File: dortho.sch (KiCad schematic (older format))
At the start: 129 parts, among them SW1 SW_Push, U1 ATmega32U4-AU, Y1 16MHz

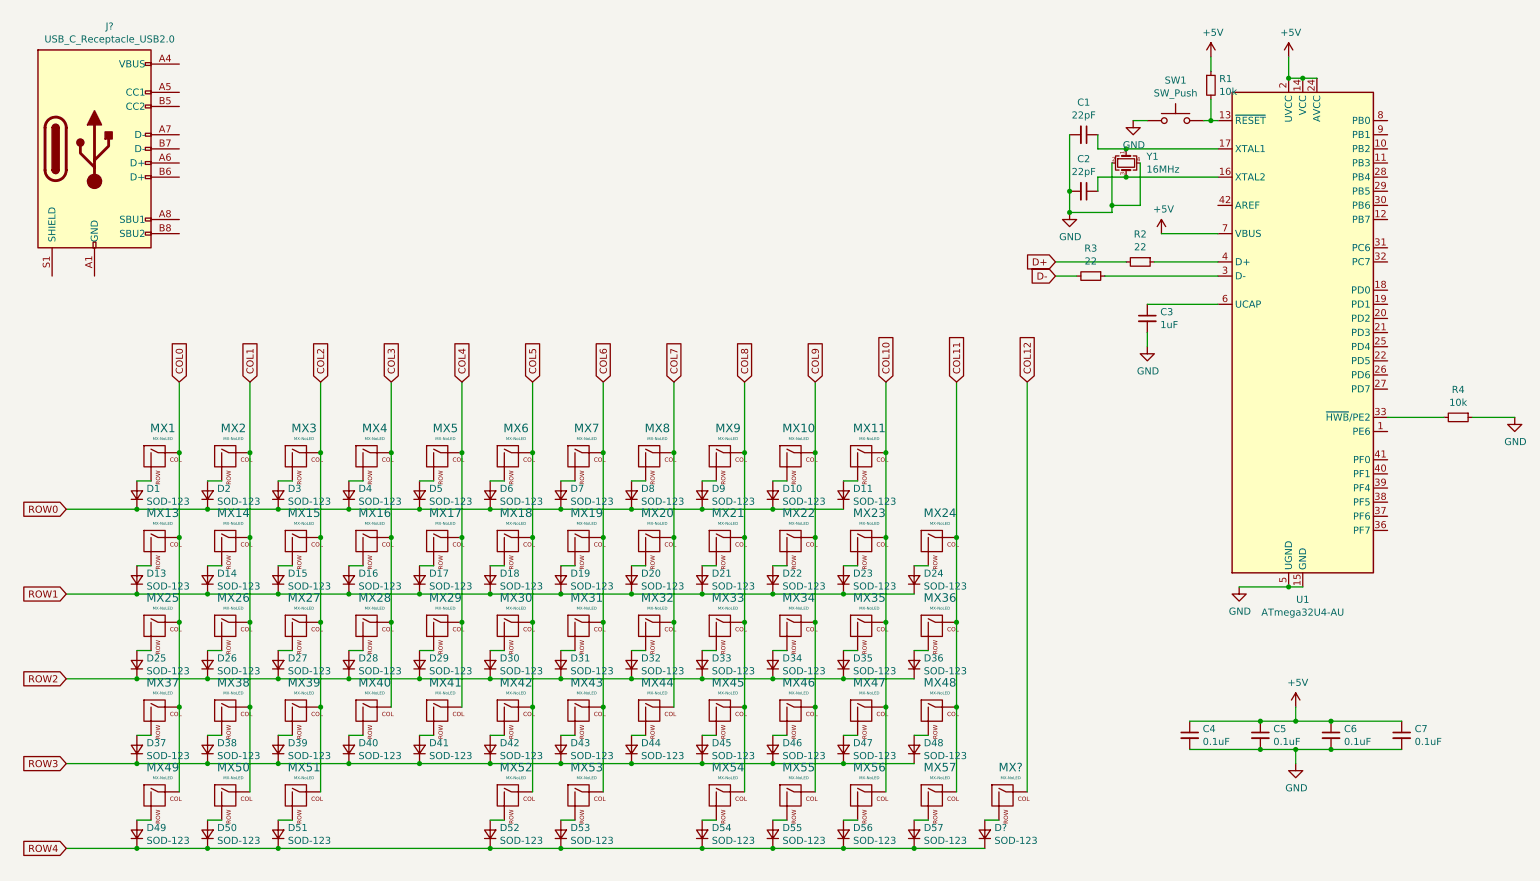
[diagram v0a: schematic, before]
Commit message: Clear switch matrix
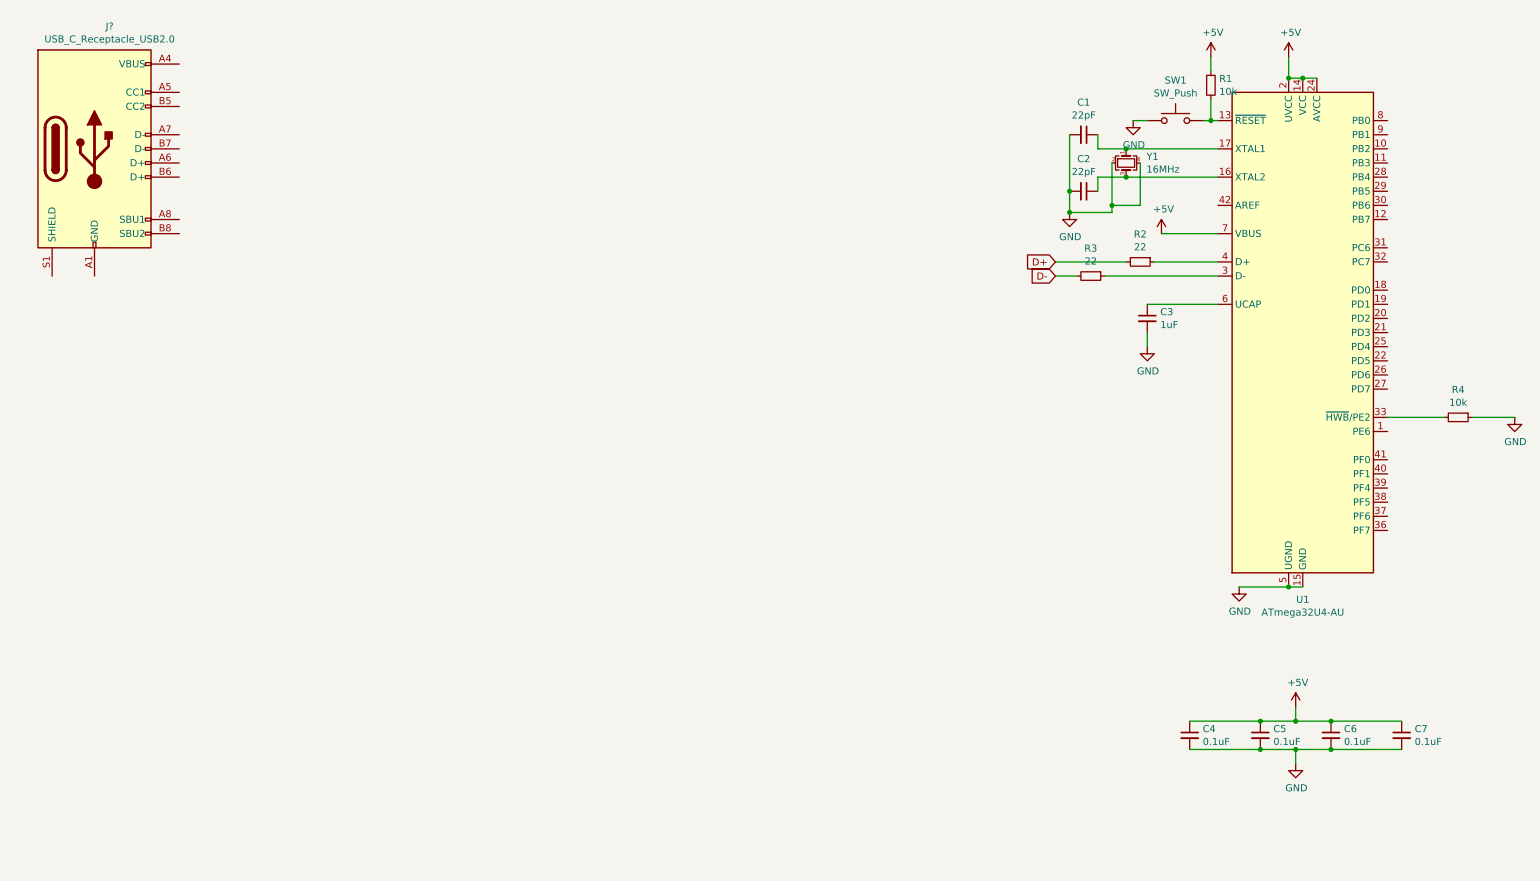
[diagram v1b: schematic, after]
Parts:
- removed D1, D10, D11, D13, D14, D15, D16, D17, D18, D19, D2, D20, D21, D22, D23, D24, D25, D26, D27, D28, D29, D3, D30, D31, D32, D33, D34, D35, D36, D37, D38, D39, D4, D40, D41, D42, D43, D44, D45, D46, D47, D48, D49, D5, D50, D51, D52, D53, D54, D55, D56, D57, D6, D7, D8, D9, D?: SOD-123, Diode_SMD:D_SOD-123, symbol Device:D_Small
- removed MX1, MX10, MX11, MX13, MX14, MX15, MX16, MX17, MX18, MX19, MX2, MX20, MX21, MX22, MX23, MX24, MX25, MX26, MX27, MX28, MX29, MX3, MX30, MX31, MX32, MX33, MX34, MX35, MX36, MX37, MX38, MX39, MX4, MX40, MX41, MX42, MX43, MX44, MX45, MX46, MX47, MX48, MX49, MX5, MX50, MX51, MX52, MX53, MX54, MX55, MX56, MX57, MX6, MX7, MX8, MX9, MX?: MX-NoLED, MX_Alps_Hybrid:MX-1U-NoLED, symbol MX_Alps_Hybrid:MX-NoLED

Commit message: Finish switch matrix
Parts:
- added D? (x73): D_Small, symbol Device:D_Small
- added MX? (x73): MX-NoLED, symbol MX_Alps_Hybrid:MX-NoLED
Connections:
- new net: D?.2 (A), MX?.2 (ROW) (x73)
- new net COL0: MX?.1 (COL), MX?.1 (COL), MX?.1 (COL), MX?.1 (COL), MX?.1 (COL)
- new net COL1: MX?.1 (COL), MX?.1 (COL), MX?.1 (COL), MX?.1 (COL), MX?.1 (COL)
- new net COL10: MX?.1 (COL), MX?.1 (COL), MX?.1 (COL), MX?.1 (COL), MX?.1 (COL)
- new net COL11: MX?.1 (COL), MX?.1 (COL), MX?.1 (COL), MX?.1 (COL), MX?.1 (COL)
- new net COL12: MX?.1 (COL), MX?.1 (COL), MX?.1 (COL), MX?.1 (COL), MX?.1 (COL)
- new net COL13: MX?.1 (COL), MX?.1 (COL), MX?.1 (COL), MX?.1 (COL), MX?.1 (COL)
- new net COL14: MX?.1 (COL), MX?.1 (COL), MX?.1 (COL), MX?.1 (COL)
- new net COL2: MX?.1 (COL), MX?.1 (COL), MX?.1 (COL), MX?.1 (COL), MX?.1 (COL)
- new net COL3: MX?.1 (COL), MX?.1 (COL), MX?.1 (COL), MX?.1 (COL), MX?.1 (COL)
- new net COL4: MX?.1 (COL), MX?.1 (COL), MX?.1 (COL), MX?.1 (COL), MX?.1 (COL)
- new net COL5: MX?.1 (COL), MX?.1 (COL), MX?.1 (COL), MX?.1 (COL), MX?.1 (COL)
- new net COL6: MX?.1 (COL), MX?.1 (COL), MX?.1 (COL), MX?.1 (COL)
- new net COL7: MX?.1 (COL), MX?.1 (COL), MX?.1 (COL), MX?.1 (COL), MX?.1 (COL)
- new net COL8: MX?.1 (COL), MX?.1 (COL), MX?.1 (COL), MX?.1 (COL), MX?.1 (COL)
- new net COL9: MX?.1 (COL), MX?.1 (COL), MX?.1 (COL), MX?.1 (COL), MX?.1 (COL)
- new net ROW0: D?.1 (K), D?.1 (K), D?.1 (K), D?.1 (K), D?.1 (K), D?.1 (K), D?.1 (K), D?.1 (K), D?.1 (K), D?.1 (K), D?.1 (K), D?.1 (K), D?.1 (K), D?.1 (K), D?.1 (K)
- new net ROW1: D?.1 (K), D?.1 (K), D?.1 (K), D?.1 (K), D?.1 (K), D?.1 (K), D?.1 (K), D?.1 (K), D?.1 (K), D?.1 (K), D?.1 (K), D?.1 (K), D?.1 (K), D?.1 (K), D?.1 (K)
- new net ROW2: D?.1 (K), D?.1 (K), D?.1 (K), D?.1 (K), D?.1 (K), D?.1 (K), D?.1 (K), D?.1 (K), D?.1 (K), D?.1 (K), D?.1 (K), D?.1 (K), D?.1 (K), D?.1 (K), D?.1 (K)
- new net ROW3: D?.1 (K), D?.1 (K), D?.1 (K), D?.1 (K), D?.1 (K), D?.1 (K), D?.1 (K), D?.1 (K), D?.1 (K), D?.1 (K), D?.1 (K), D?.1 (K), D?.1 (K), D?.1 (K), D?.1 (K)
- new net ROW4: D?.1 (K), D?.1 (K), D?.1 (K), D?.1 (K), D?.1 (K), D?.1 (K), D?.1 (K), D?.1 (K), D?.1 (K), D?.1 (K), D?.1 (K), D?.1 (K), D?.1 (K)

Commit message: Finishing with type C
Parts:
- added D?: D_Schottky, symbol Device:D_Schottky
- added FB?: Ferrite_Bead_Small, symbol Device:Ferrite_Bead_Small
- added R? (x2): 5.1k, symbol Device:R
- added TH?: Thermistor, symbol Device:Thermistor
- added U?: USBLC6-2SC6, Package_TO_SOT_SMD:SOT-23-6, symbol Power_Protection:USBLC6-2SC6
- gave numbers to parts that had none: 147
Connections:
- net +5V: now also J1.A4 (VBUS), J1.A9 (VBUS), J1.B4 (VBUS), J1.B9 (VBUS), D?.1 (K), TH?.2, U?.5 (VBUS)
- net D+: now also J1.A7 (D-), J1.B7 (D-)
- net D-: now also J1.A6 (D+), J1.B6 (D+)
- net GND: now also J1.A1 (GND), J1.A12 (GND), J1.B1 (GND), J1.B12 (GND), FB?.1, R?.1, R?.1, U?.2 (GND)
- net at J1.A5 (CC1): now also R?.2
- net at J1.B5 (CC2): now also R?.2
- net at J1.S1 (SHIELD): now also FB?.2
- new net: D?.2 (A), TH?.1

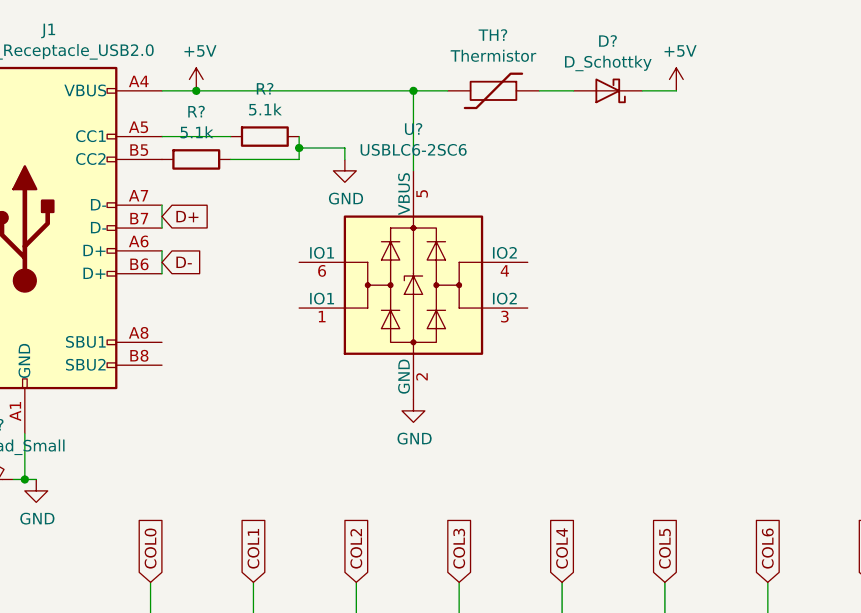
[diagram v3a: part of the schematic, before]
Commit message: Finish type C connection
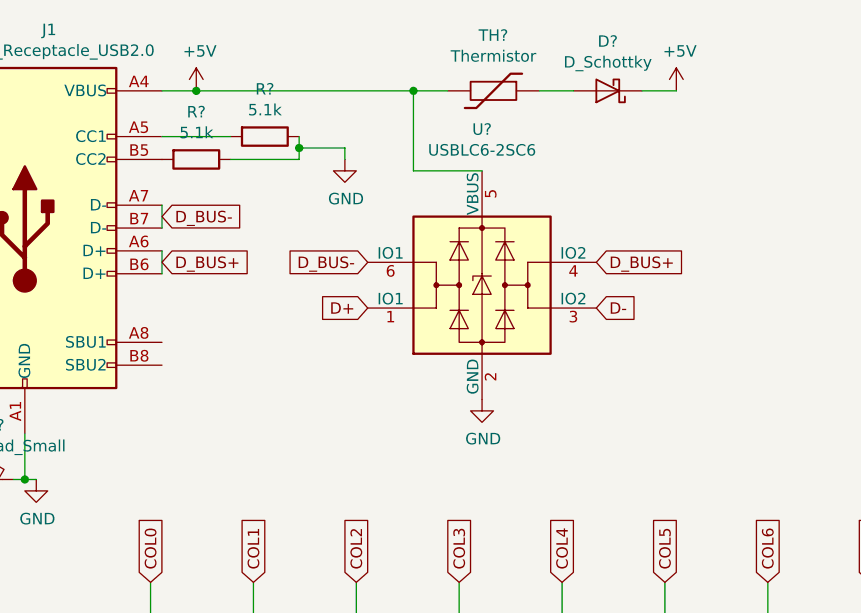
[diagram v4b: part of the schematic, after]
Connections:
- net D+: now also U?.1 (IO1); no longer J1.A7 (D-), J1.B7 (D-)
- net D-: now also U?.3 (IO2); no longer J1.A6 (D+), J1.B6 (D+)
- net D_BUS+: now reaches U?.4 (IO2)
- net D_BUS+: now also J1.A6 (D+), J1.B6 (D+)
- net D_BUS-: now reaches U?.6 (IO1)
- net D_BUS-: now also J1.A7 (D-), J1.B7 (D-)
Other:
- moved on the sheet: U?
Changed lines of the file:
@@
 	1    0    0    -1
 $EndComp
-$Comp
-L Power_Protection:USBLC6-2SC6 U?
-U 1 1 630D6912
-P 2700 1700
-F 0 "U?" H 2700 2381 50  0000 C CNN
-F 1 "USBLC6-2SC6" H 2700 2290 50  0000 C CNN
-F 2 "Package_TO_SOT_SMD:SOT-23-6" H 1950 2100 50  0001 C CNN
-F 3 "http://www2.st.com/resource/en/datasheet/CD00050750.pdf" H 2900 2050 50  0001 C CNN
-	1    2700 1700
-	1    0    0    -1
-$EndComp
-Text GLabel 1600 1600 2    50   Input ~ 0
-D-
 Wire Wire Line
 	1600 1550 1600 1650
-Text GLabel 1600 1400 2    50   Input ~ 0
-D+
 Wire Wire Line
 	1600 1350 1600 1450
@@
 	0    1    1    0
 $EndComp
-Wire Wire Line
-	1750 850  2700 850
 Connection ~ 1750 850
-Wire Wire Line
-	2700 1200 2700 850
-Connection ~ 2700 850
-Wire Wire Line
-	2700 850  2850 850
-$Comp
-L power:GND #PWR?
-U 1 1 632ED364
-P 2700 2200
-F 0 "#PWR?" H 2700 1950 50  0001 C CNN
-F 1 "GND" H 2705 2027 50  0000 C CNN
-F 2 "" H 2700 2200 50  0001 C CNN
-F 3 "" H 2700 2200 50  0001 C CNN
-	1    2700 2200
-	1    0    0    -1
-$EndComp
 $Comp
 L Device:D_Schottky D?
@@
 Wire Wire Line
 	3700 850  3850 850
+Text GLabel 1600 1400 2    50   Input ~ 0
+D_BUS-
+Text GLabel 1600 1600 2    50   Input ~ 0
+D_BUS+
+Connection ~ 2700 850
+Wire Wire Line
+	2700 850  2850 850
+Wire Wire Line
+	1750 850  2700 850
+Wire Wire Line
+	2700 1200 2700 850
+Wire Wire Line
+	2700 1200 3000 1200
+Text GLabel 3500 1600 2    50   Input ~ 0
+D_BUS+
+Text GLabel 2500 1600 0    50   Input ~ 0
+D_BUS-
+$Comp
+L power:GND #PWR?
+U 1 1 632ED364
+P 3000 2200
+F 0 "#PWR?" H 3000 1950 50  0001 C CNN
+F 1 "GND" H 3005 2027 50  0000 C CNN
+F 2 "" H 3000 2200 50  0001 C CNN
+F 3 "" H 3000 2200 50  0001 C CNN
+	1    3000 2200
+	1    0    0    -1
+$EndComp
+Text GLabel 2500 1800 0    50   Input ~ 0
+D+
+Text GLabel 3500 1800 2    50   Input ~ 0
+D-
+$Comp
+L Power_Protection:USBLC6-2SC6 U?
+U 1 1 630D6912
+P 3000 1700
+F 0 "U?" H 3000 2381 50  0000 C CNN
+F 1 "USBLC6-2SC6" H 3000 2290 50  0000 C CNN
+F 2 "Package_TO_SOT_SMD:SOT-23-6" H 2250 2100 50  0001 C CNN
+F 3 "http://www2.st.com/resource/en/datasheet/CD00050750.pdf" H 3200 2050 50  0001 C CNN
+	1    3000 1700
+	1    0    0    -1
+$EndComp
 $EndSCHEMATC

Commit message: Modify VCC
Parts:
- gave numbers to parts that had none: 6
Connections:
- net +5V: no longer U1.14 (VCC), U1.2 (UVCC), U1.24 (AVCC), U1.34 (VCC), U1.44 (AVCC)
- net COL0: now also U1.22 (PD5)
- net COL1: now also U1.25 (PD4)
- net COL10: now also U1.37 (PF6)
- net COL11: now also U1.38 (PF5)
- net COL12: now also U1.39 (PF4)
- net COL13: now also U1.40 (PF1)
- net COL14: now also U1.41 (PF0)
- net COL2: now also U1.26 (PD6)
- net COL3: now also U1.27 (PD7)
- net COL4: now also U1.28 (PB4)
- net COL5: now also U1.29 (PB5)
- net COL6: now also U1.30 (PB6)
- net COL7: now also U1.31 (PC6)
- net COL8: now also U1.32 (PC7)
- net COL9: now also U1.36 (PF7)
- net ROW0: now also U1.1 (PE6)
- net ROW1: now also U1.8 (PB0)
- net ROW2: now also U1.9 (PB1)
- net ROW3: now also U1.10 (PB2)
- net ROW4: now also U1.11 (PB3)
- new net: U1.14 (VCC), U1.2 (UVCC), U1.24 (AVCC), U1.34 (VCC), U1.44 (AVCC)
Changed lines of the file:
@@
 L power:+5V #PWR0101
 U 1 1 624280D8
-P 9450 800
-F 0 "#PWR0101" H 9450 650 50  0001 C CNN
-F 1 "+5V" H 9465 973 50  0000 C CNN
-F 2 "" H 9450 800 50  0001 C CNN
-F 3 "" H 9450 800 50  0001 C CNN
-	1    9450 800
-	1    0    0    -1
-$EndComp
-Wire Wire Line
-	9450 800  9450 950
+P 9450 700
+F 0 "#PWR0101" H 9450 550 50  0001 C CNN
+F 1 "+5V" H 9465 873 50  0000 C CNN
+F 2 "" H 9450 700 50  0001 C CNN
+F 3 "" H 9450 700 50  0001 C CNN
+	1    9450 700
+	1    0    0    -1
+$EndComp
 Wire Wire Line
 	9450 950  9550 950
-Connection ~ 9450 950
 Connection ~ 9550 950
 Wire Wire Line
@@
 COL14
 $Comp
-L Device:Ferrite_Bead_Small FB?
+L Device:Ferrite_Bead_Small FB1
 U 1 1 63076E1C
 P 850 2550
-F 0 "FB?" V 613 2550 50  0000 C CNN
+F 0 "FB1" V 613 2550 50  0000 C CNN
 F 1 "Ferrite_Bead_Small" V 704 2550 50  0000 C CNN
 F 2 "" V 780 2550 50  0001 C CNN
@@
 	1000 2550 1000 2350
 $Comp
-L power:GND #PWR?
+L power:GND #PWR0111
 U 1 1 630BB391
 P 1050 2550
-F 0 "#PWR?" H 1050 2300 50  0001 C CNN
+F 0 "#PWR0111" H 1050 2300 50  0001 C CNN
 F 1 "GND" H 1055 2377 50  0000 C CNN
 F 2 "" H 1050 2550 50  0001 C CNN
@@
 Connection ~ 1000 2550
 $Comp
-L power:+5V #PWR?
+L power:+5V #PWR0112
 U 1 1 630D5634
 P 1750 850
-F 0 "#PWR?" H 1750 700 50  0001 C CNN
+F 0 "#PWR0112" H 1750 700 50  0001 C CNN
 F 1 "+5V" H 1765 1023 50  0000 C CNN
 F 2 "" H 1750 850 50  0001 C CNN
@@
 	1600 1350 1600 1450
 $Comp
-L Device:R R?
+L Device:R R6
 U 1 1 6310C819
 P 1750 1150
-F 0 "R?" V 1543 1150 50  0000 C CNN
+F 0 "R6" V 1543 1150 50  0000 C CNN
 F 1 "5.1k" V 1634 1150 50  0000 C CNN
 F 2 "" V 1680 1150 50  0001 C CNN
@@
 $EndComp
 $Comp
-L power:GND #PWR?
+L power:GND #PWR0113
 U 1 1 63152C8B
 P 2400 1150
-F 0 "#PWR?" H 2400 900 50  0001 C CNN
+F 0 "#PWR0113" H 2400 900 50  0001 C CNN
 F 1 "GND" H 2405 977 50  0000 C CNN
 F 2 "" H 2400 1150 50  0001 C CNN
@@
 	1600 1050 1900 1050
 $Comp
-L Device:R R?
+L Device:R R5
 U 1 1 632317B5
 P 2050 1050
-F 0 "R?" V 1843 1050 50  0000 C CNN
+F 0 "R5" V 1843 1050 50  0000 C CNN
 F 1 "5.1k" V 1934 1050 50  0000 C CNN
 F 2 "" V 1980 1050 50  0001 C CNN
@@
 	1600 850  1750 850
 $Comp
-L Device:Thermistor TH?
+L Device:Thermistor TH1
 U 1 1 632A0E6E
 P 3050 850
-F 0 "TH?" V 2808 850 50  0000 C CNN
+F 0 "TH1" V 2808 850 50  0000 C CNN
 F 1 "Thermistor" V 2899 850 50  0000 C CNN
 F 2 "" H 3050 850 50  0001 C CNN
@@
 Connection ~ 1750 850
 $Comp
-L Device:D_Schottky D?
+L Device:D_Schottky D74
 U 1 1 632EE5EF
 P 3550 850
-F 0 "D?" H 3550 634 50  0000 C CNN
+F 0 "D74" H 3550 634 50  0000 C CNN
 F 1 "D_Schottky" H 3550 725 50  0000 C CNN
 F 2 "" H 3550 850 50  0001 C CNN
@@
 	3250 850  3400 850
 $Comp
-L power:+5V #PWR?
+L power:+5V #PWR0114
 U 1 1 6330D6C2
 P 3850 850
-F 0 "#PWR?" H 3850 700 50  0001 C CNN
+F 0 "#PWR0114" H 3850 700 50  0001 C CNN
 F 1 "+5V" H 3865 1023 50  0000 C CNN
 F 2 "" H 3850 850 50  0001 C CNN
@@
 D_BUS-
 $Comp
-L power:GND #PWR?
+L power:GND #PWR0115
 U 1 1 632ED364
 P 3000 2200
-F 0 "#PWR?" H 3000 1950 50  0001 C CNN
+F 0 "#PWR0115" H 3000 1950 50  0001 C CNN
 F 1 "GND" H 3005 2027 50  0000 C CNN
 F 2 "" H 3000 2200 50  0001 C CNN
@@
 D-
 $Comp
-L Power_Protection:USBLC6-2SC6 U?
+L Power_Protection:USBLC6-2SC6 U2
 U 1 1 630D6912
 P 3000 1700
-F 0 "U?" H 3000 2381 50  0000 C CNN
+F 0 "U2" H 3000 2381 50  0000 C CNN
 F 1 "USBLC6-2SC6" H 3000 2290 50  0000 C CNN
 F 2 "Package_TO_SOT_SMD:SOT-23-6" H 2250 2100 50  0001 C CNN
@@
 	1    0    0    -1
 $EndComp
+Text GLabel 10150 3650 2    50   Input ~ 0
+COL14
+Text GLabel 10150 3750 2    50   Input ~ 0
+COL13
+Text GLabel 10150 3850 2    50   Input ~ 0
+COL12
+Text GLabel 10150 3950 2    50   Input ~ 0
+COL11
+Text GLabel 10150 4050 2    50   Input ~ 0
+COL10
+Text GLabel 10150 4150 2    50   Input ~ 0
+COL9
+Text GLabel 10150 2250 2    50   Input ~ 0
+COL8
+Text GLabel 10150 2150 2    50   Input ~ 0
+COL7
+Text GLabel 10150 1850 2    50   Input ~ 0
+COL6
+Text GLabel 10150 1750 2    50   Input ~ 0
+COL5
+Text GLabel 10150 1650 2    50   Input ~ 0
+COL4
+Text GLabel 10150 3150 2    50   Input ~ 0
+COL3
+Text GLabel 10150 3050 2    50   Input ~ 0
+COL2
+Text GLabel 10150 2850 2    50   Input ~ 0
+COL1
+Text GLabel 10150 2950 2    50   Input ~ 0
+COL0
+Text GLabel 10150 3450 2    50   Input ~ 0
+ROW0
+Text GLabel 10150 1250 2    50   Input ~ 0
+ROW1
+Text GLabel 10150 1350 2    50   Input ~ 0
+ROW2
+Text GLabel 10150 1450 2    50   Input ~ 0
+ROW3
+Text GLabel 10150 1550 2    50   Input ~ 0
+ROW4
+Wire Wire Line
+	9450 900  9450 950
+Connection ~ 9450 950
 $EndSCHEMATC
